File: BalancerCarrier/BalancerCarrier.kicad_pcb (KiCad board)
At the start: 4 copper layers, 50 x 53.6 mm, 36 parts, among them J3 MAG+ / MAG- PTH, J4 GPS MODULE 3V3 UART, J5 OPTICAL HEAD 7-WAY, SW1 ACQUIRE, U1 FeatherS3[D], U2 LM1815MX/NOPB, U3 SN74LVC1G132DBVR, U4 SN74LVC1G123DCTR, U5 IIS3DWBTR

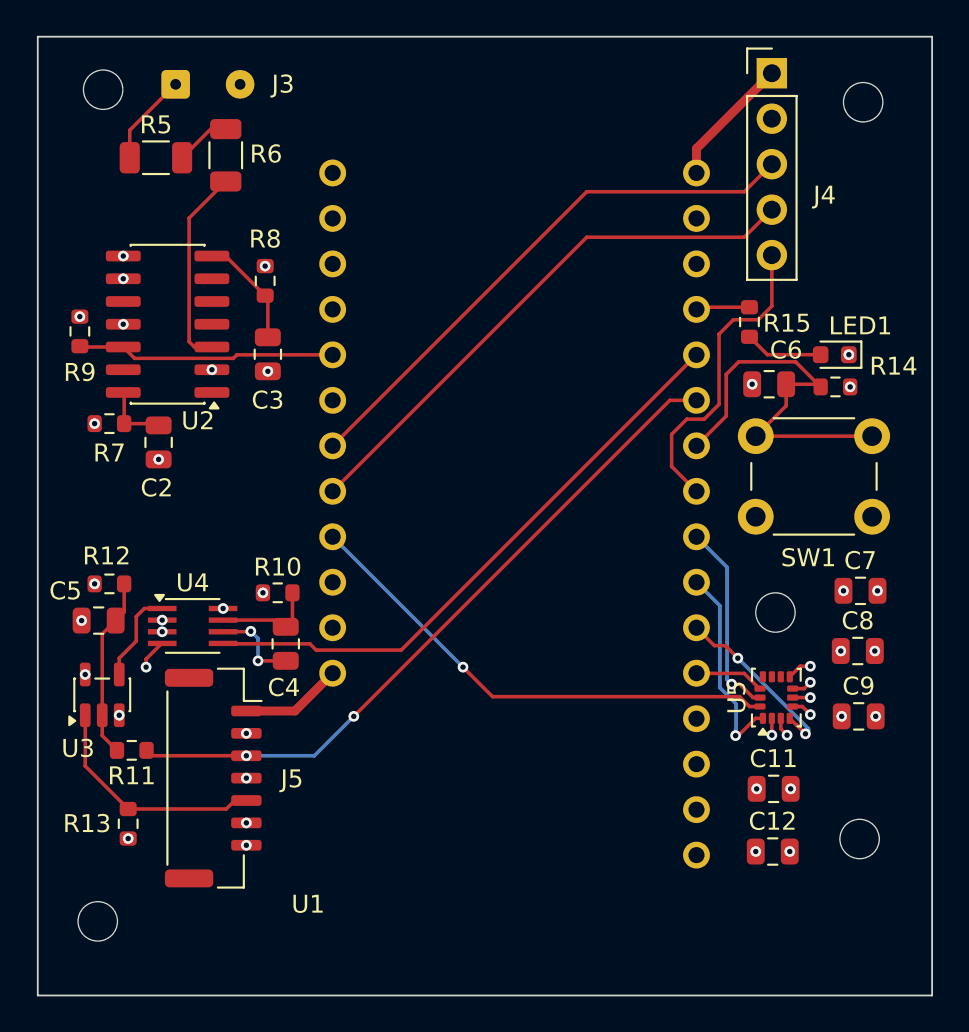
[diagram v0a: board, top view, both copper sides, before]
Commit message: feat: carrier J5 moved toward the optical head; head gain redistributed
Carrier: J5 moved up the left edge, next to the optical head, clear of the
FeatherS3[D] battery connector, opening away from the module. Each J5 ground
pin and 3V3 now drops to its plane through its own via within ~2 mm, and
OPT_COMP no longer runs alongside OPT_LED_EN. DRC 0 violations, 0
unconnected, 0 schematic parity (with the local U5 LGA pad-to-pad rule).

Optical head: R21 10k -> 4.99k, R23 120k -> 240k, C21 22p -> 47p C0G. Same
~120 kOhm total gain with about twice the TIA ambient headroom (~160 to
~320 uA photocurrent), per the 2026-09-23 SPICE review; to be bench-tested
before production. Silkscreen cleanup clears the previous DRC warnings.
DRC 0 violations, 0 unconnected; the 3 parity items are mounting holes and
fiducials without symbols.

Co-Authored-By: Claude Opus 5.5 <noreply@anthropic.com>
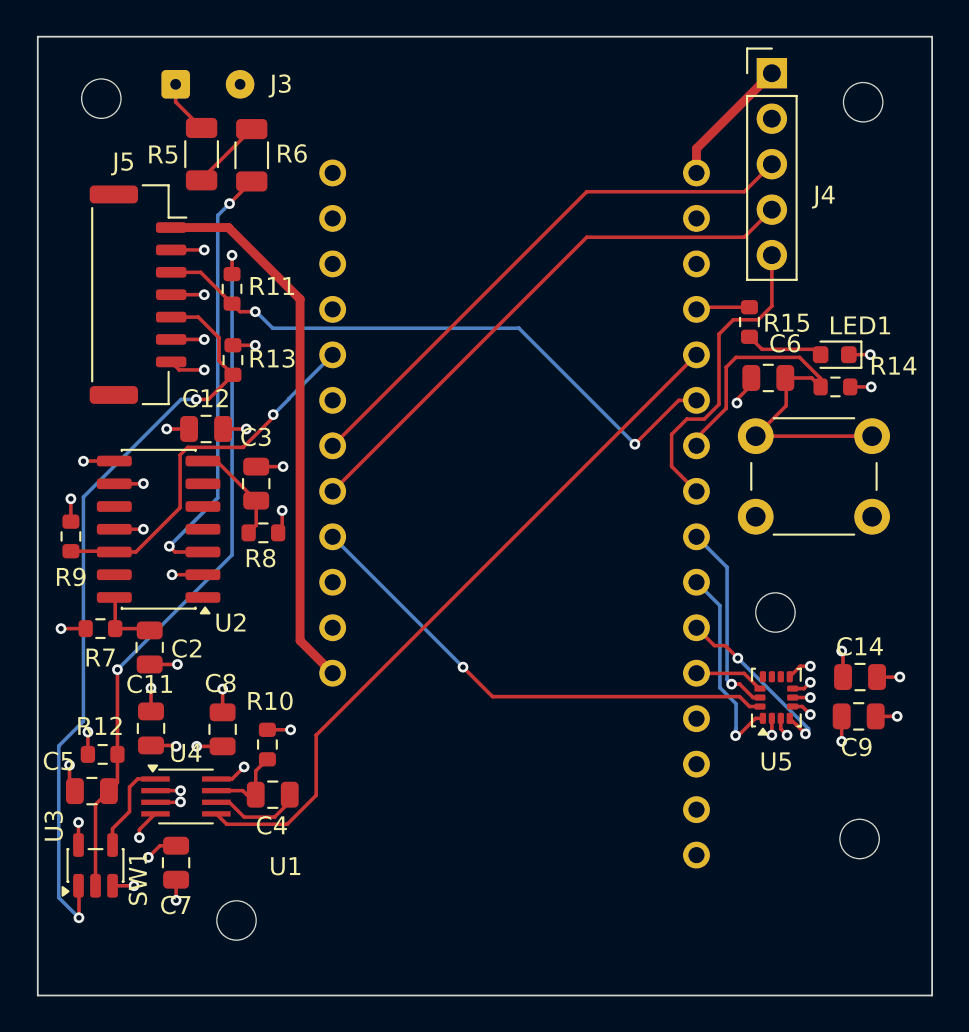
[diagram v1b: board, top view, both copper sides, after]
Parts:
- added C14: 100n, Capacitor_SMD:C_0805_2012Metric, F.Cu at (117.5, 87.6)
- moved C7 41.1 mm to (79.3, 97.9), turned to -90 degrees
- moved C12 39.5 mm to (81.0, 73.7)
- moved C8 35.7 mm to (81.9, 90.5), turned to 90 degrees
- moved C11 34.9 mm to (77.9, 90.4), turned to 90 degrees
- moved J5 27.3 mm to (77.2, 66.2)
- moved R13 26.6 mm to (82.5, 69.8), turned to 90 degrees
- moved R11 26.4 mm to (82.4, 65.9), turned to 90 degrees
- moved R8 14.1 mm to (84.2, 79.5), turned to 0 degrees
- moved C2 11.5 mm to (77.8, 85.9)
- moved R9 11.5 mm to (73.4, 79.7)
- moved U2 11.5 mm to (78.3, 79.3)
- moved R7 11.5 mm to (75.0, 84.8)
- moved R12 9.53 mm to (75.2, 91.9)
- moved U3 9.53 mm to (74.8, 98.1)
- moved C5 9.53 mm to (74.6, 93.9)
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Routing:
- net GND: track 5.85 -> 36.2 mm, vias 25 -> 26
- net /OPT_COMP: track 13.0 -> 43.0 mm, vias 0 -> 2
- net /SYNC_DELAY: track 10.1 -> 39.4 mm, vias 0 -> 2
- net /VBAT: track 5.69 -> 30.5 mm
- net +3V3: track 2.57 -> 26.2 mm, vias 17 -> 18
- net Net-(U2-VR_IN): track 11.2 -> 24.3 mm, vias 0 -> 2
- net /MAG_TACH: track 14.5 -> 21.0 mm, vias 0 -> 1
- net /OPT_TACH: track 33.4 -> 39.9 mm
- net /OPT_LED_EN: track 39.1 -> 34.3 mm
- net /MAG_IN: track 5.16 -> 3.04 mm
- net /ACQUIRE_BUTTON: track 22.9 -> 24.1 mm
- net /OPT_RCEXT: track 5.71 -> 4.54 mm
- net Net-(R5-Pad2): track 3.10 -> 4.02 mm
- net /OPT_CEXT: track 4.93 -> 5.19 mm, vias 2 -> 0
